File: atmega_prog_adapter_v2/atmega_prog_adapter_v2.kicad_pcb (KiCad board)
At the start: 2 copper layers, 81.3 x 43.2 mm, 9 parts, among them J1 AVR-ISP-10, U1 ATmega48A/PA/88A/PA/168A/PA/3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, Y1 XTAL

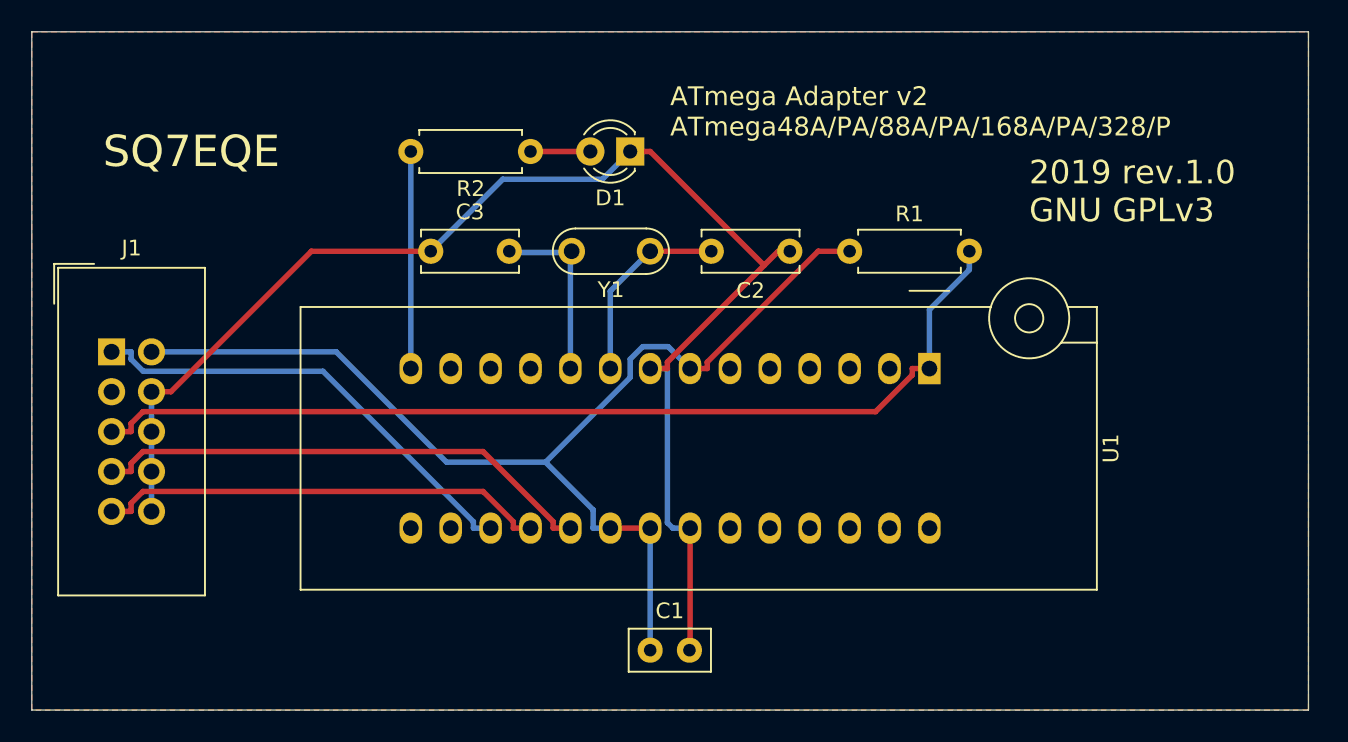
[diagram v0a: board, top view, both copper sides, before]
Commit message: update: fixed invalid margins around crystal
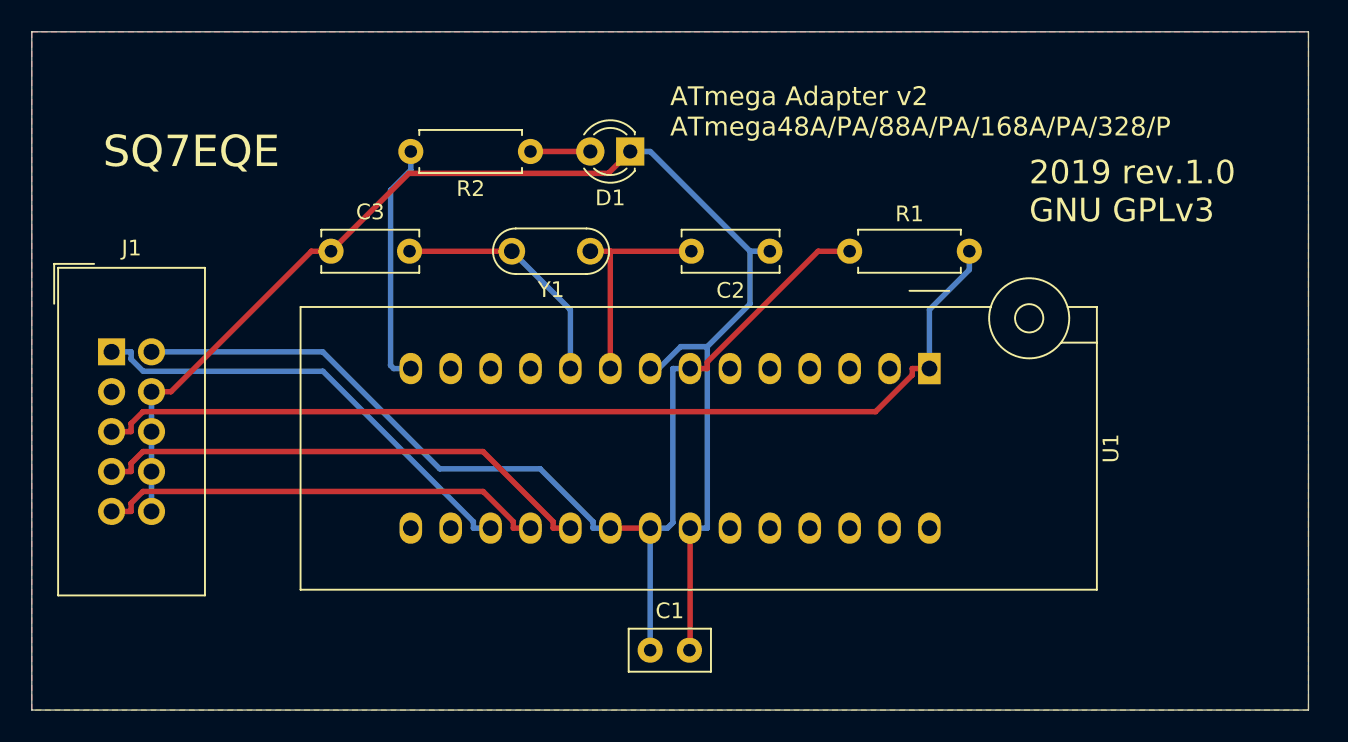
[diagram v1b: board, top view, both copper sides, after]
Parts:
- moved C3 6.35 mm to (108.0, 80.0)
- moved Y1 3.81 mm to (124.5, 80.0)
- moved C2 1.27 mm to (135.9, 80.0)
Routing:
- net /XTAL2: track 11.4 -> 15.5 mm
- net Net-(R2-Pad2): track 13.8 -> 15.5 mm
- net /XTAL1: track 12.4 -> 13.9 mm
- net Net-(C1-Pad1): track 71.9 -> 70.4 mm
- net GND: track 88.5 -> 87.8 mm
